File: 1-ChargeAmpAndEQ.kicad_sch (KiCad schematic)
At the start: 44 parts, among them J101 6.3mm stereo, J102 6.3mm stereo, U1 OPA145

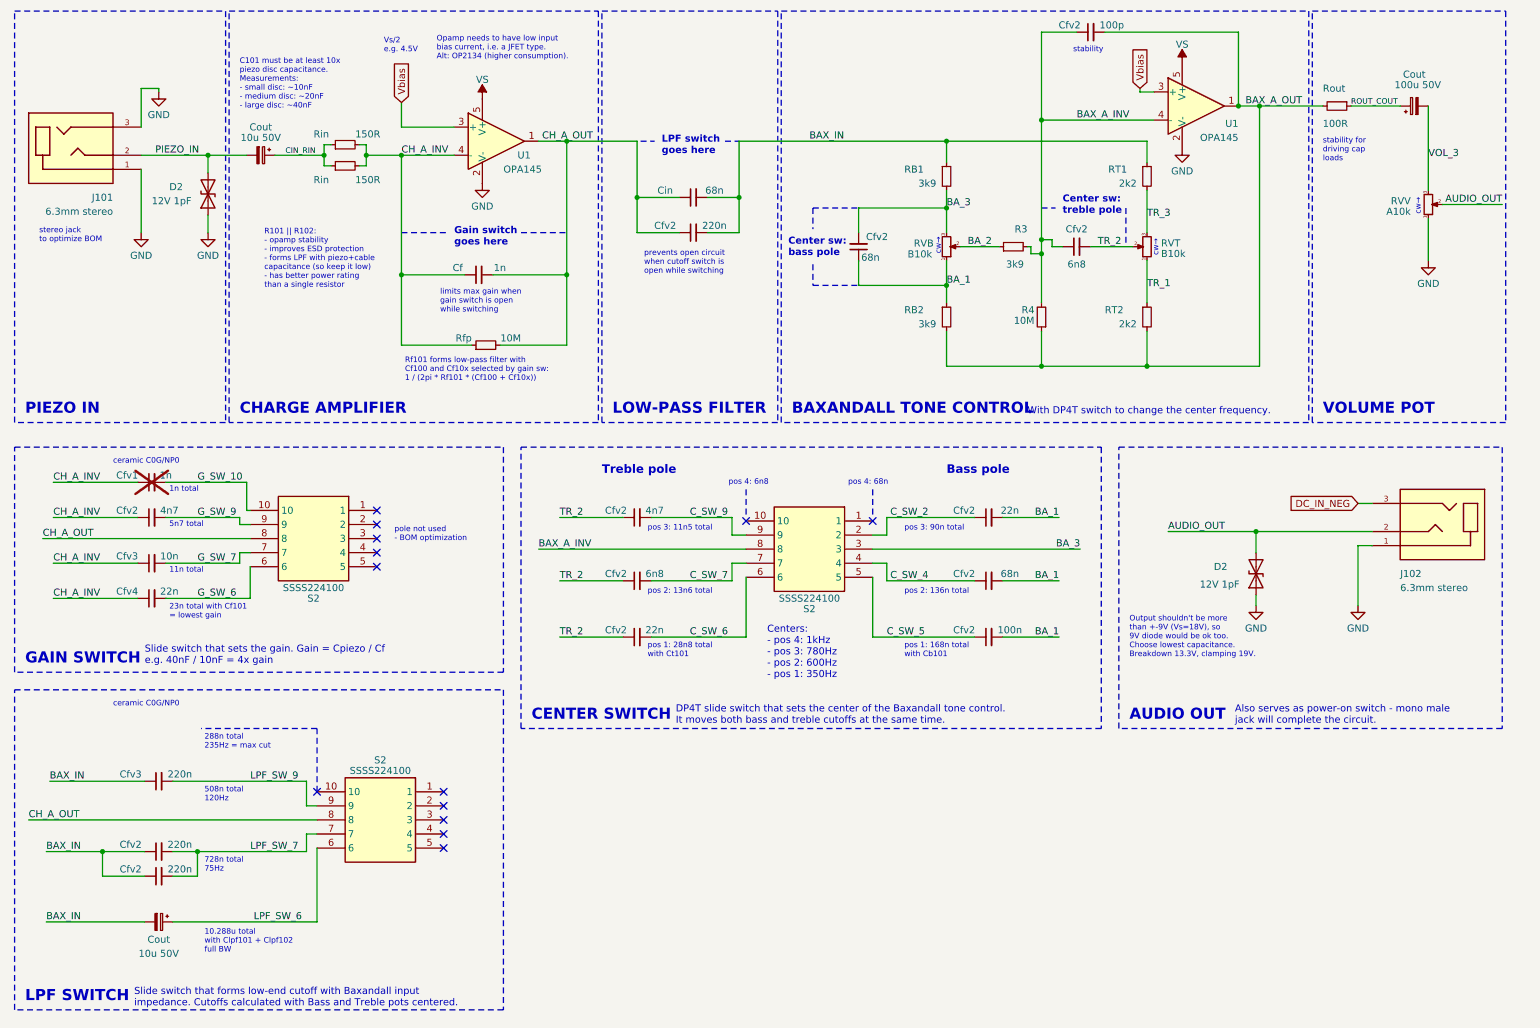
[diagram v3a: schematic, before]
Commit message: improving the schematic - v3.0. Very crude draft of board layout with battery holder underneath the PCB
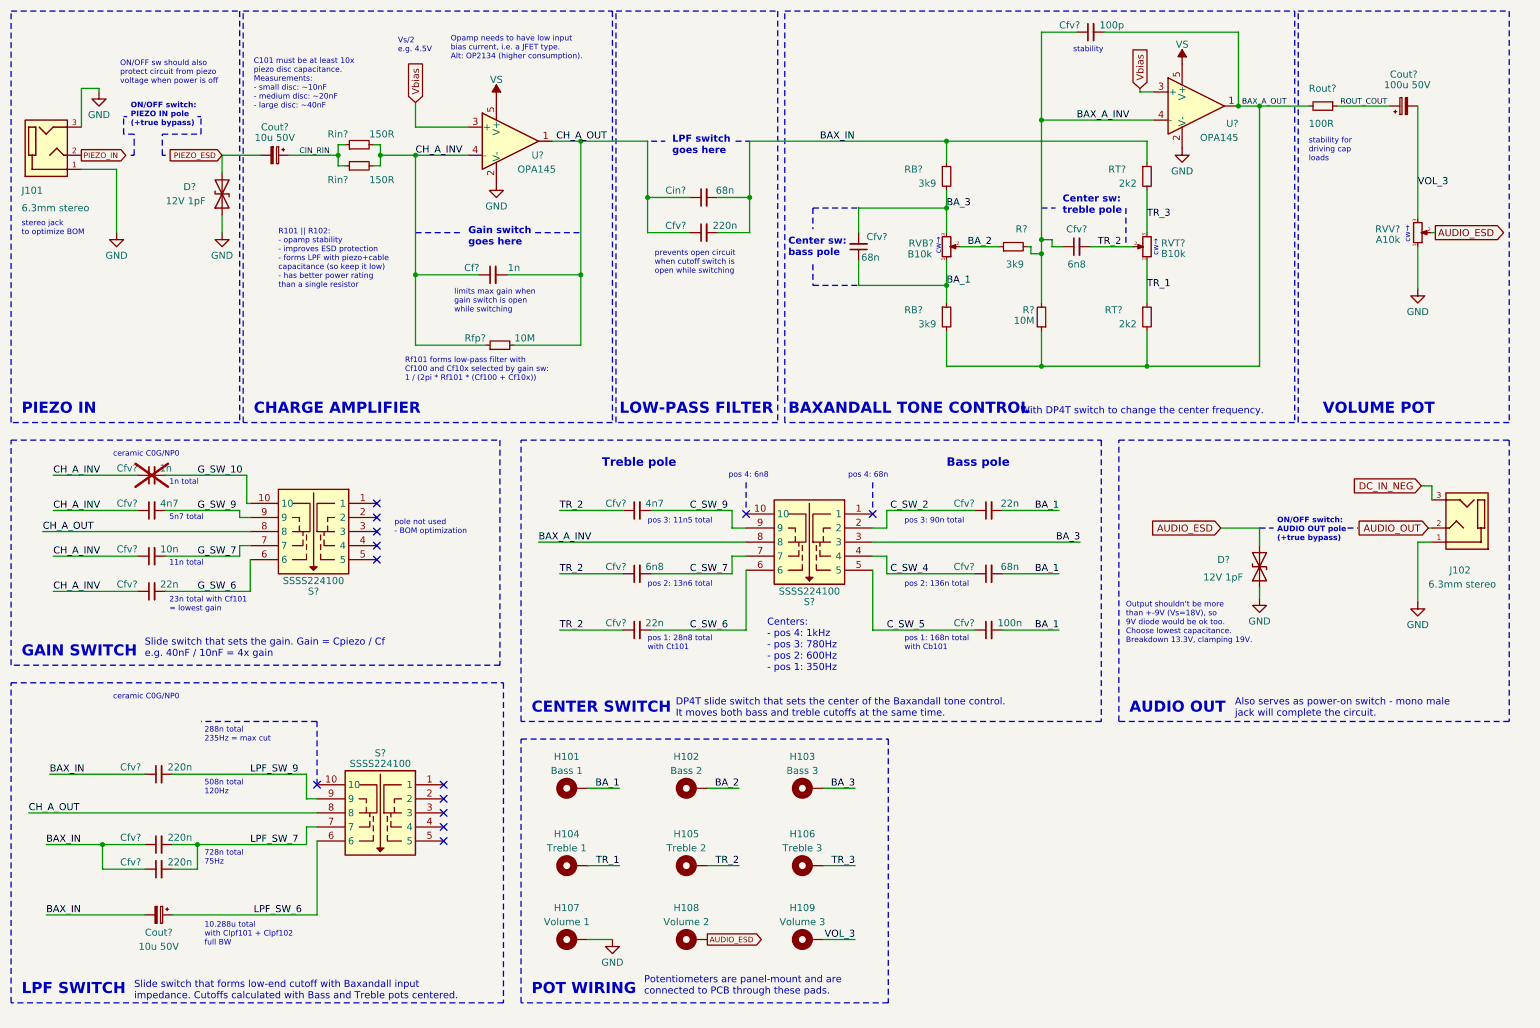
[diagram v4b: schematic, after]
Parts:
- added H101: Bass 1, library:FreePad_1.1mm_2.0mm, symbol Mechanical:MountingHole_Pad
- added H102: Bass 2, library:FreePad_1.1mm_2.0mm, symbol Mechanical:MountingHole_Pad
- added H103: Bass 3, library:FreePad_1.1mm_2.0mm, symbol Mechanical:MountingHole_Pad
- added H104: Treble 1, library:FreePad_1.1mm_2.0mm, symbol Mechanical:MountingHole_Pad
- added H105: Treble 2, library:FreePad_1.1mm_2.0mm, symbol Mechanical:MountingHole_Pad
- added H106: Treble 3, library:FreePad_1.1mm_2.0mm, symbol Mechanical:MountingHole_Pad
- added H107: Volume 1, library:FreePad_1.1mm_2.0mm, symbol Mechanical:MountingHole_Pad
- added H108: Volume 2, library:FreePad_1.1mm_2.0mm, symbol Mechanical:MountingHole_Pad
- added H109: Volume 3, library:FreePad_1.1mm_2.0mm, symbol Mechanical:MountingHole_Pad
- J101, J102: Height (none) -> 12.5mm
- RVB?: renamed from RVB; footprint library:PTV09A-4020F-A103 -> (none); Mfr Bourns -> SR Passives; Mfr Part # PTV09A-4225S-B103 -> R16148-1A-1-B10K; Mouser Part # 652-PTV09A4225SB103 -> -; TME Part # (none) -> R16148-1A-1-B10K
- RVT?: renamed from RVT; footprint library:PTV09A-4020F-A103 -> (none); Mfr Bourns -> SR Passives; Mfr Part # PTV09A-4225S-B103 -> R16148-1A-1-B10K; Mouser Part # 652-PTV09A4225SB103 -> -; TME Part # (none) -> R16148-1A-1-B10K
- RVV?: renamed from RVV; footprint library:PTV09A-4020F-A103 -> (none); Mfr Bourns -> SR Passives; Mfr Part # PTV09A-4025S-A103 -> R16148-1A-1-A10K; Mouser Part # 652-PTV09A4025SA103 -> -; TME Part # (none) -> R16148-1A-1-A10K
- renumbered Cf to Cf?, Cfv2 to Cfv?, Cfv3 to Cfv?, Cfv4 to Cfv?, Cfv1 to Cfv?, Cin to Cin?, Cout to Cout?, D2 to D?, R3 to R?, R4 to R?, RB2 to RB?, RB1 to RB?, RT2 to RT?, RT1 to RT?, Rfp to Rfp?, Rin to Rin?, Rout to Rout?, S2 to S?, U1 to U?
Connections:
- net AUDIO_OUT: no longer D?.2 (A2), RVV?.2
- net BA_1: now also H101.1
- net BA_2: now also H102.1
- net BA_3: now also H103.1
- net GND: now also H107.1
- net PIEZO_IN: no longer Cout?.2, D?.2 (A2)
- net TR_1: now also H104.1
- net TR_2: now also H105.1
- net TR_3: now also H106.1
- net VOL_3: now also H109.1
- new net AUDIO_ESD: D?.2 (A2), H108.1, RVV?.2
- new net PIEZO_ESD: Cout?.2, D?.2 (A2)
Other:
- note added: "ON/OFF sw should also protect circuit from piezo voltage when power is off"
- note added: "ON/OFF switch: AUDIO OUT pole (+true bypass)"
- note added: "ON/OFF switch: PIEZO IN pole (+true bypass)"
- note added: "POT WIRING"
- note added: "Potentiometers are panel-mount and are connected to PCB through these pads."
- moved on the sheet: Cf?, Cfv?, Cin?, Cout?, D?, J101, J102, RVV?, Rfp?, Rin?, Rout?, U?

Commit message: working on component placement, improving schematics
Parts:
- Cout?: value 10u 50V -> 0.47u; footprint library:EEEFK1H100UR -> library:GRM31C5C1E474JE01L; symbol Device:C_Polarized_Small -> Device:C_Small; LCSC Part # C178547 -> C6049896; Mfr Panasonic -> Murata; Mfr Part # EEEFK1H100UR -> GRM31C5C1E474JE01L; Mouser Part # 667-EEE-FK1H100UR -> 81-GRM31C5C1E474JE1L; Purpose AC coupling / DC blocking -> AC coupling / DC blocking. Should be at least 10x piezo cap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; Source (none) -> Mouser; TME Part # (none) -> GRM31C5C1E474JE01L
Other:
- note added: "C101 must be at least 10x piezo disc capacitance. Measurements: - small disc: ~10nF - medium disc: ~20nF - large disc: ~40nF Too much capacitance will charge very slowly (through Rf101 = 10M) and will cause DC on input."
- note removed: "C101 must be at least 10x piezo disc capacitance. Measurements: - small disc: ~10nF - medium disc: ~20nF - large disc: ~40nF"
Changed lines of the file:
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@@
     (effects (font (size 1.27 1.27)) (justify left bottom))
   )
-  (text "C101 must be at least 10x \npiezo disc capacitance.\nMeasurements:\n- small disc: ~10nF\n- medium disc: ~20nF\n- large disc: ~40nF"
-    (at 57.15 33.02 0)
+  (text "C101 must be at least 10x \npiezo disc capacitance.\nMeasurements:\n- small disc: ~10nF\n- medium disc: ~20nF\n- large disc: ~40nF\nToo much capacitance will\ncharge very slowly (through \nRf101 = 10M) and will cause \nDC on input."
+    (at 56.515 33.655 0)
     (effects (font (size 1 1)) (justify left bottom))
   )
@@
     )
   )
-  (symbol (lib_id "Device:C_Polarized_Small") (at 60.96 41.275 270) (unit 1)
-    (in_bom yes) (on_board no) (dnp no)
+  (symbol (lib_id "Device:C_Small") (at 60.96 41.275 270) (unit 1)
+    (in_bom yes) (on_board yes) (dnp no)
     (property "Reference" "Cout?" (at 60.96 36.195 90)
       (effects (font (size 1.27 1.27)))
     )
-    (property "Value" "10u 50V" (at 60.96 38.1 90)
-      (effects (font (size 1.27 1.27)))
-    )
-    (property "Footprint" "library:EEEFK1H100UR" (at 60.96 41.275 0)
-      (effects (font (size 1.27 1.27)) hide)
-    )
-    (property "Datasheet" "https://cz.mouser.com/datasheet/2/315/ABA0000C1181-947564.pdf" (at 60.96 41.275 0)
-      (effects (font (size 1.27 1.27)) hide)
-    )
-    (property "Purpose" "AC coupling / DC blocking" (at 60.96 41.275 0)
-      (effects (font (size 1.27 1.27)) hide)
-    )
-    (property "LCSC Part #" "C178547" (at 60.96 41.275 0)
-      (effects (font (size 1.27 1.27)) hide)
-    )
-    (property "Mouser Part #" "667-EEE-FK1H100UR" (at 60.96 41.275 0)
-      (effects (font (size 1.27 1.27)) hide)
-    )
-    (property "Mfr Part #" "EEEFK1H100UR" (at 60.96 41.275 0)
-      (effects (font (size 1.27 1.27)) hide)
-    )
-    (property "Mfr" "Panasonic" (at 60.96 41.275 0)
-      (effects (font (size 1.27 1.27)) hide)
-    )
-    (property "TME Part #" "" (at 60.96 41.275 0)
-      (effects (font (size 1.27 1.27)) hide)
-    )
-    (property "Source" "" (at 60.96 41.275 0)
-      (effects (font (size 1.27 1.27)) hide)
-    )
+    (property "Value" "0.47u" (at 60.96 38.1 90)
+      (effects (font (size 1.27 1.27)))
+    )
+    (property "Footprint" "library:GRM31C5C1E474JE01L" (at 60.96 41.275 0)
+      (effects (font (size 1.27 1.27)) hide)
+    )
+    (property "Datasheet" "https://cz.mouser.com/datasheet/2/281/1/GRM31C5C1E474JE01_01A-1987703.pdf" (at 60.96 41.275 0)
+      (effects (font (size 1.27 1.27)) hide)
+    )
+    (property "Purpose" "AC coupling / DC blocking. Should be at least 10x piezo capacitance" (at 60.96 41.275 0)
+      (effects (font (size 1.27 1.27)) hide)
+    )
+    (property "LCSC Part #" "C6049896" (at 60.96 41.275 0)
+      (effects (font (size 1.27 1.27)) hide)
+    )
+    (property "Mouser Part #" "81-GRM31C5C1E474JE1L" (at 60.96 41.275 0)
+      (effects (font (size 1.27 1.27)) hide)
+    )
+    (property "Mfr Part #" "GRM31C5C1E474JE01L" (at 60.96 41.275 0)
+      (effects (font (size 1.27 1.27)) hide)
+    )
+    (property "Mfr" "Murata" (at 60.96 41.275 0)
+      (effects (font (size 1.27 1.27)) hide)
+    )
+    (property "TME Part #" "GRM31C5C1E474JE01L" (at 60.96 41.275 0)
+      (effects (font (size 1.27 1.27)) hide)
+    )
+    (property "Source" "Mouser" (at 60.96 41.275 0)
+      (effects (font (size 1.27 1.27)) hide)
+    )

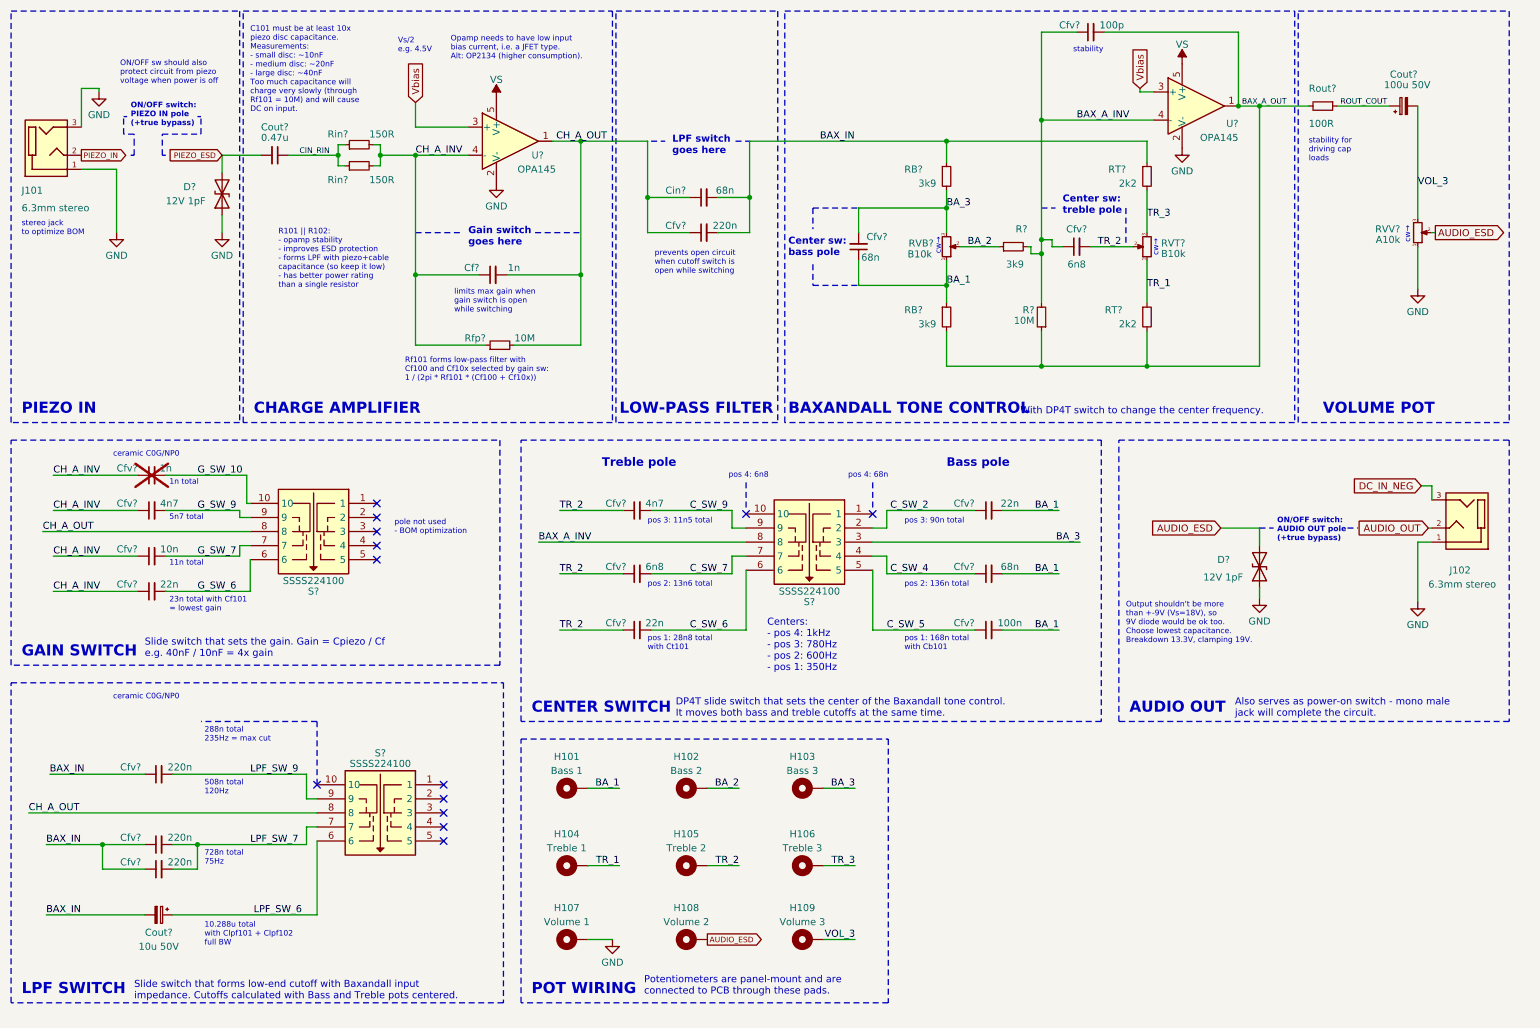
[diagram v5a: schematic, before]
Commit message: saving in Kicad8 for the first time - some underlying formats changed
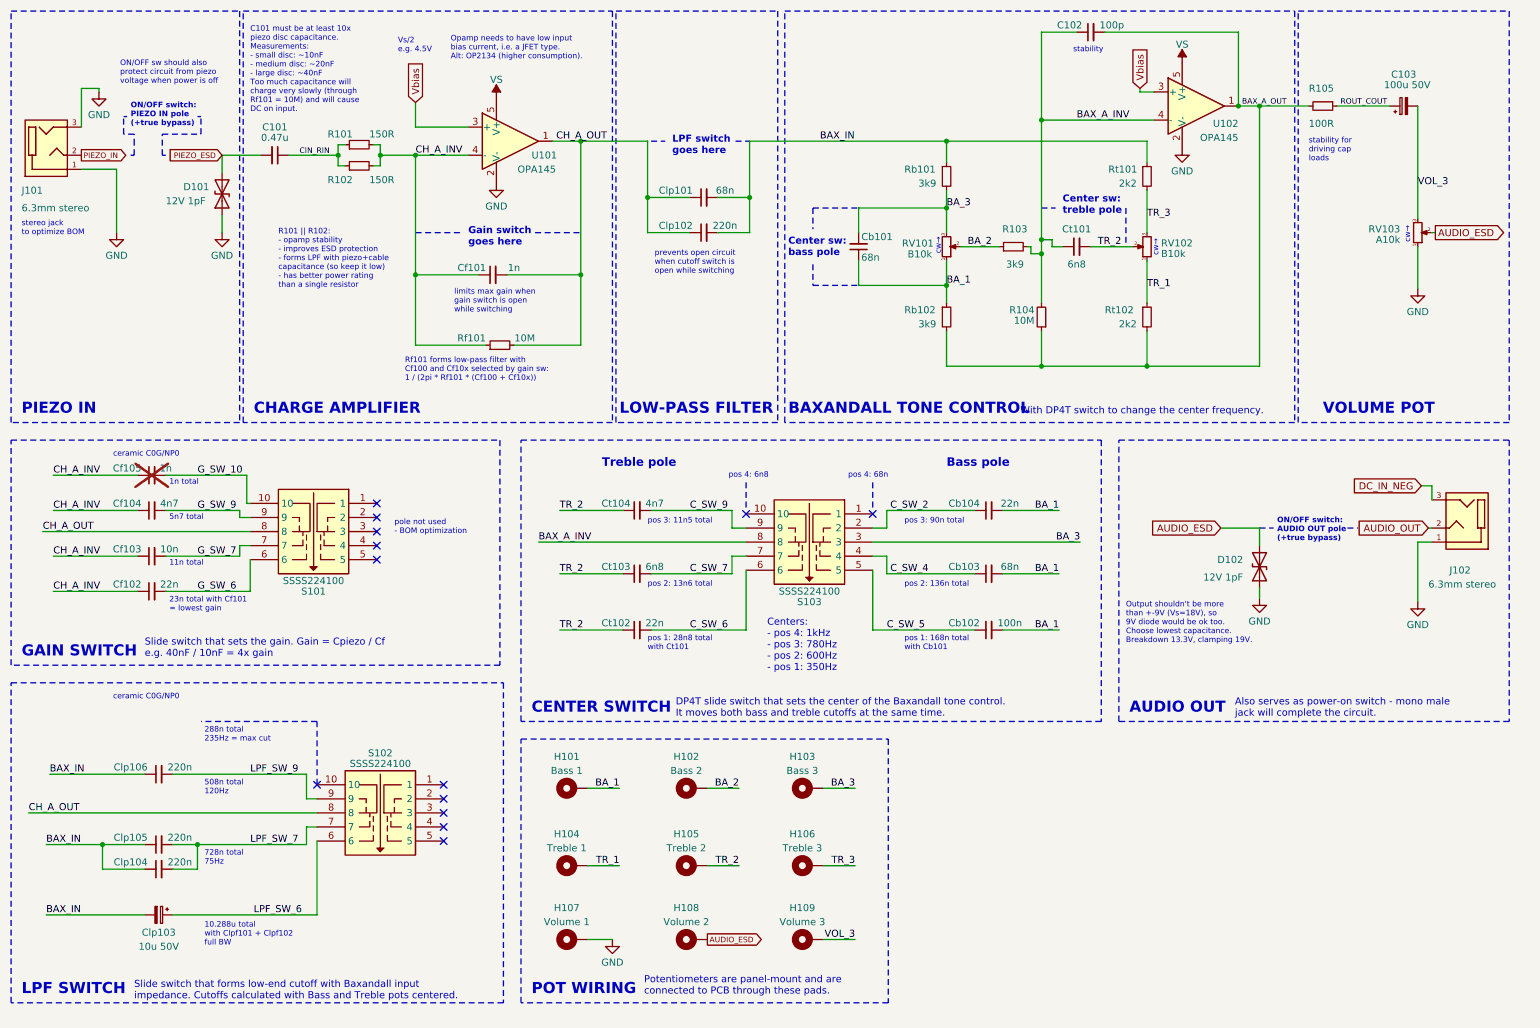
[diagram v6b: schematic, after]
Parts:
- gave numbers to parts that had none: 42
